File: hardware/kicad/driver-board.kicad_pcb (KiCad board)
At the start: 4 copper layers, 42.2 x 36.8 mm, 55 parts, among them J1 Conn_01x13_Male, U1 TXS0108E, U2 ME6210A30M3G, U3 ME6210A33M3G, U4 TLV61046ADB, U5 NC7SZ125, U6 FT813, U7 ER-TFT040-2, X1 YSX321SL

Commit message: Update footprints for machine assembly
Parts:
- U6: footprint Package_DFN_QFN:QFN-56-1EP_8x8mm_P0.5mm_EP5.6x5.6mm_HandSolder -> Package_DFN_QFN:QFN-56-1EP_8x8mm_P0.5mm_EP5.6x5.6mm
- U7: footprint Connector_FFC-FPC:TE_5-1734839-0_1x60-1MP_P0.5mm_Horizontal_HandSolder -> kicad:HRS_FH28-60S-0.5SH(05)
- moved U7 2.35 mm to (145.7, 66.4)
- moved C12 1.43 mm to (127.8, 76.6)
- moved C13 1.43 mm to (128.8, 77.7)
- moved C11 1.43 mm to (126.7, 75.5)
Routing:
- net GND: track 109.0 -> 125.8 mm, vias 38 -> 41
- net +3V3: track 41.2 -> 30.5 mm, vias 2 -> 3
- net SDI_BUFFER: track 12.0 -> 13.1 mm
- net PCLK: track 27.6 -> 28.7 mm
- net DE: track 28.6 -> 29.6 mm
- net R7: track 11.2 -> 12.2 mm
- net R2: track 9.33 -> 10.3 mm
- net G2: track 9.95 -> 10.9 mm
- net G3: track 9.57 -> 10.6 mm
- net FTRES: track 22.8 -> 23.8 mm
- net R3: track 9.70 -> 10.7 mm
- net G4: track 9.20 -> 10.2 mm
- net B6: track 11.4 -> 12.4 mm
- net B5: track 11.8 -> 12.8 mm
- net B1: track 15.5 -> 16.5 mm
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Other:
- board size 42.2 x 36.8 mm -> 42.8 x 36.8 mm
- board text added: "REV2007E"
- board text removed: "REV2007D"

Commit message: Add OSHW logo
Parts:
- added OSHW Logo: OSHW-Logo2_9.8x8mm_SilkScreen, Symbol:OSHW-Logo2_9.8x8mm_SilkScreen, B.Cu at (131.0, 61.0)

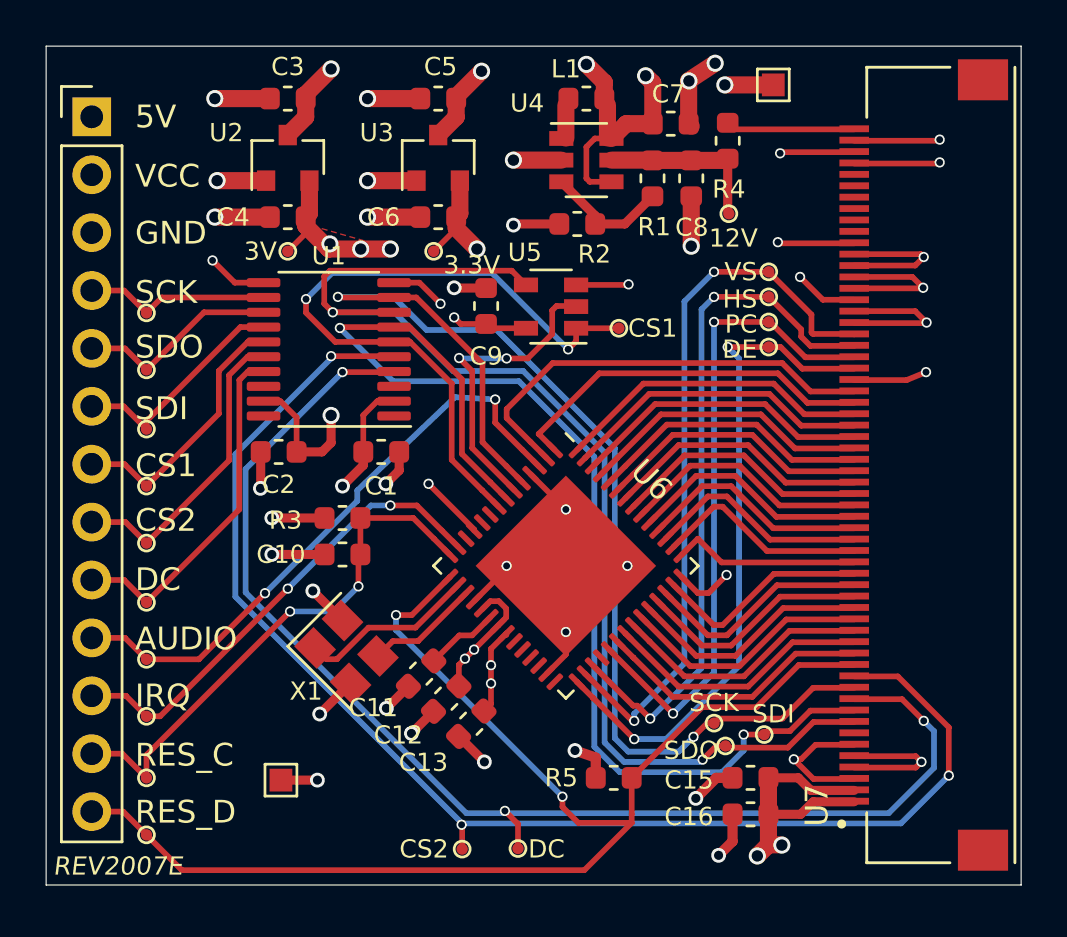
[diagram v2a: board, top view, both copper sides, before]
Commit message: Clean up board and expose less debug signals
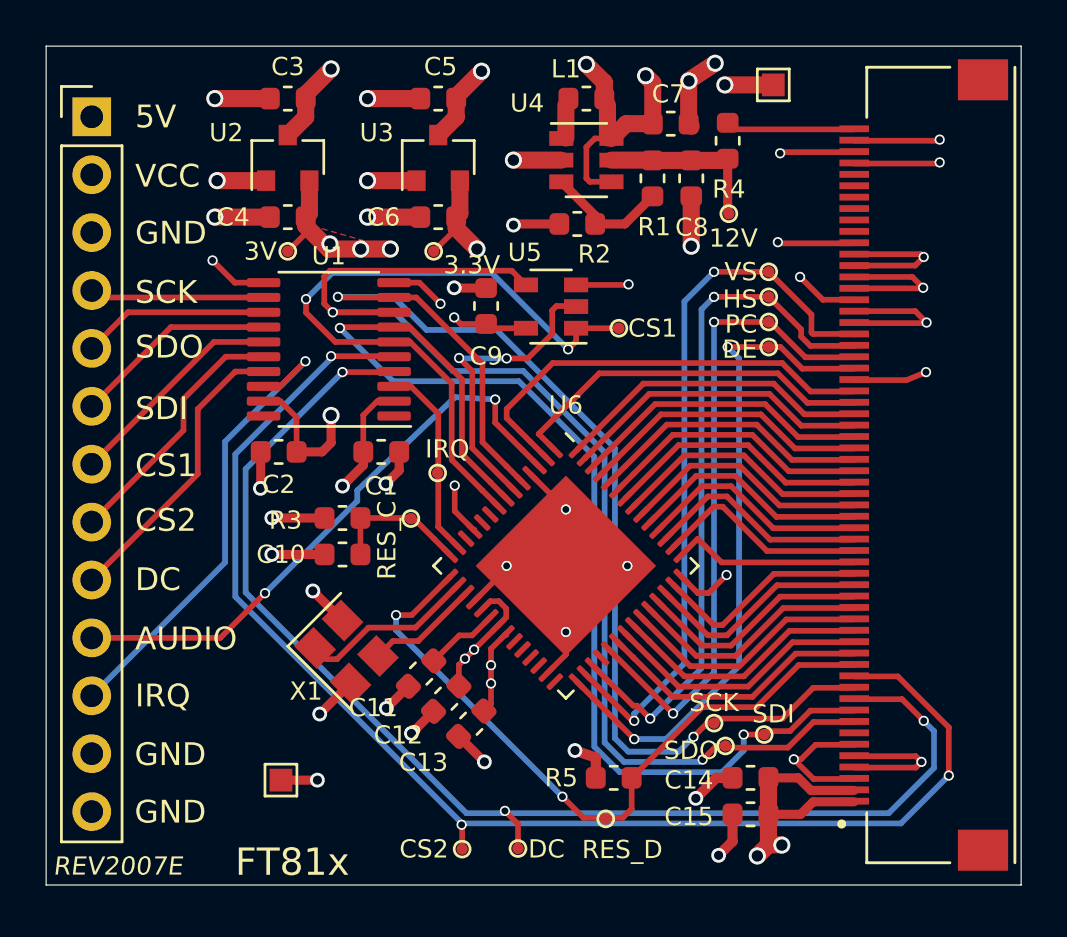
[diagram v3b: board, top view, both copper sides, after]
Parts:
- removed the TP10 at (114.6, 69.8)
- removed the TP12 at (114.6, 72.4)
- removed the TP14 at (114.6, 62.2)
- removed the TP16 at (114.6, 64.8)
- removed TP19, TP21, TP24, TP25: TestPoint, TestPoint:TestPoint_Pad_D0.5mm
- removed the TP6 at (114.6, 59.7)
- removed the TP8 at (114.6, 67.3)
- added IRQ: TestPoint, TestPoint:TestPoint_Pad_D0.5mm, F.Cu at (127.4, 66.7)
- added RES_C: TestPoint, TestPoint:TestPoint_Pad_D0.5mm, F.Cu at (126.2, 68.7)
- added RES_D: TestPoint, TestPoint:TestPoint_Pad_D0.5mm, F.Cu at (134.8, 81.9)
- moved OSHW Logo 1.02 mm to (131.0, 62.0)
- renumbered C15 to C14, C16 to C15, TP11 to TP10, TP22 to TP11, TP13 to TP12, TP23 to TP13, TP15 to TP14, TP17 to TP16, TP4 to TP2, TP2 to TP3, TP5 to TP4, TP3 to TP5, TP7 to TP6, TP18 to TP7, TP9 to TP8, TP20 to TP9
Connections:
- J1 pad 12: FTRES -> GND
- J1 pad 13: DISPRES -> GND
- U1 pad 18: Net-(U1-Pad18) -> IRQ
- U1 pad 3: Net-(U1-Pad3) -> IRQ_3V
- U6 pad 13: IRQ -> IRQ_3V
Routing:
- net DISPRES: track 57.2 -> 30.8 mm
- net FTRES: track 23.8 -> 6.32 mm, vias 2 -> 0
- net IRQ_3V: track 0.00 -> 8.63 mm
- net DC: track 15.5 -> 13.0 mm
- net CS2: track 13.9 -> 11.8 mm
- net CS1: track 11.7 -> 9.76 mm
- net SDO: track 10.0 -> 8.98 mm
- net SCK: track 8.65 -> 7.66 mm
- net AUDIO: track 26.8 -> 26.0 mm
- net SDI: track 8.97 -> 8.19 mm
- net +3V0: track 47.7 -> 47.2 mm
- net IRQ: track 21.0 -> 20.9 mm, vias 2 -> 1
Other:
- board text added: "FT81x"
- board text removed: "RES_C"
- board text removed: "RES_D"
